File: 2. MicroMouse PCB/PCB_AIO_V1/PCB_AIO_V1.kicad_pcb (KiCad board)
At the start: 2 copper layers, 70 x 70 mm, 57 parts, among them J1 Conn_01x02_Pin, J10 Conn_01x03_Pin, J11 Conn_01x03_Pin, J12 Conn_01x03_Pin, J13 Conn_01x06_Pin, J14 Conn_01x06_Pin, J15 Conn_01x06_Pin, J16 Conn_01x06_Pin, J2 STLINK, J3 MPU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

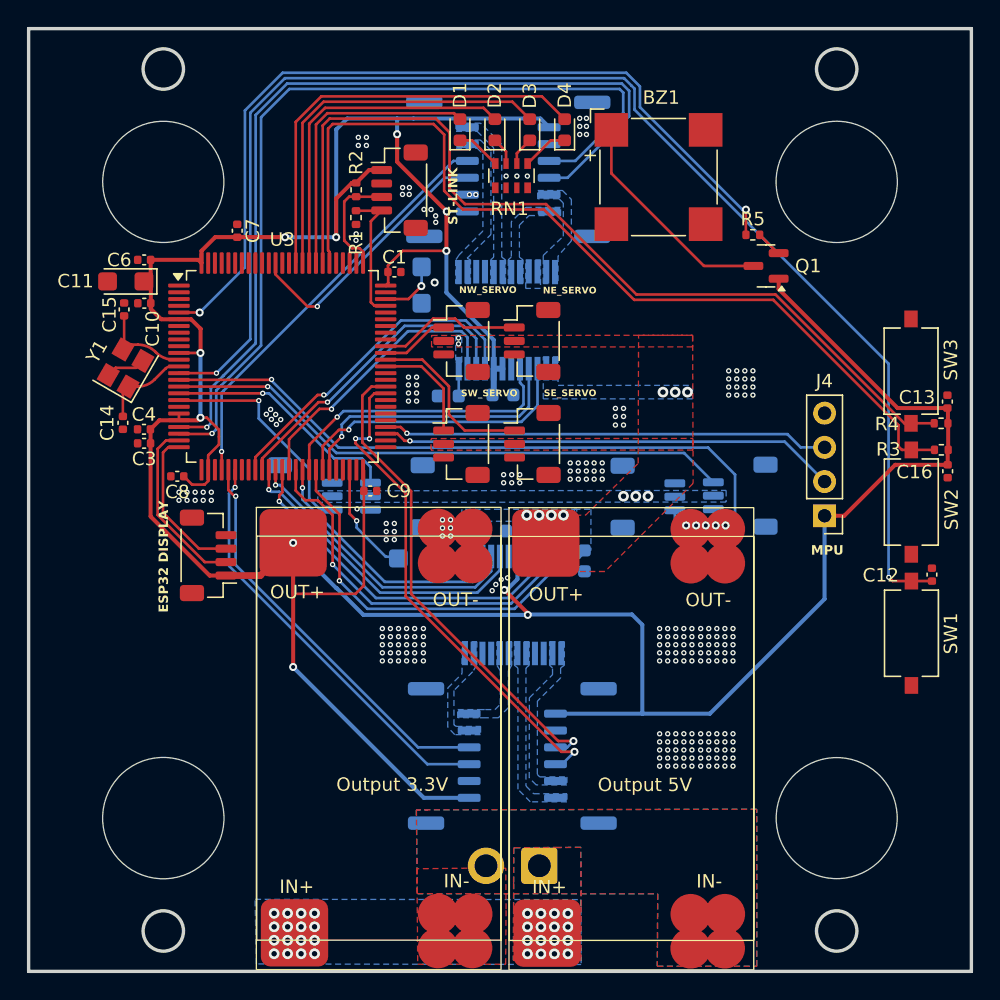
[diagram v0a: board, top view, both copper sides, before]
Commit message: moved stm32h743vit6
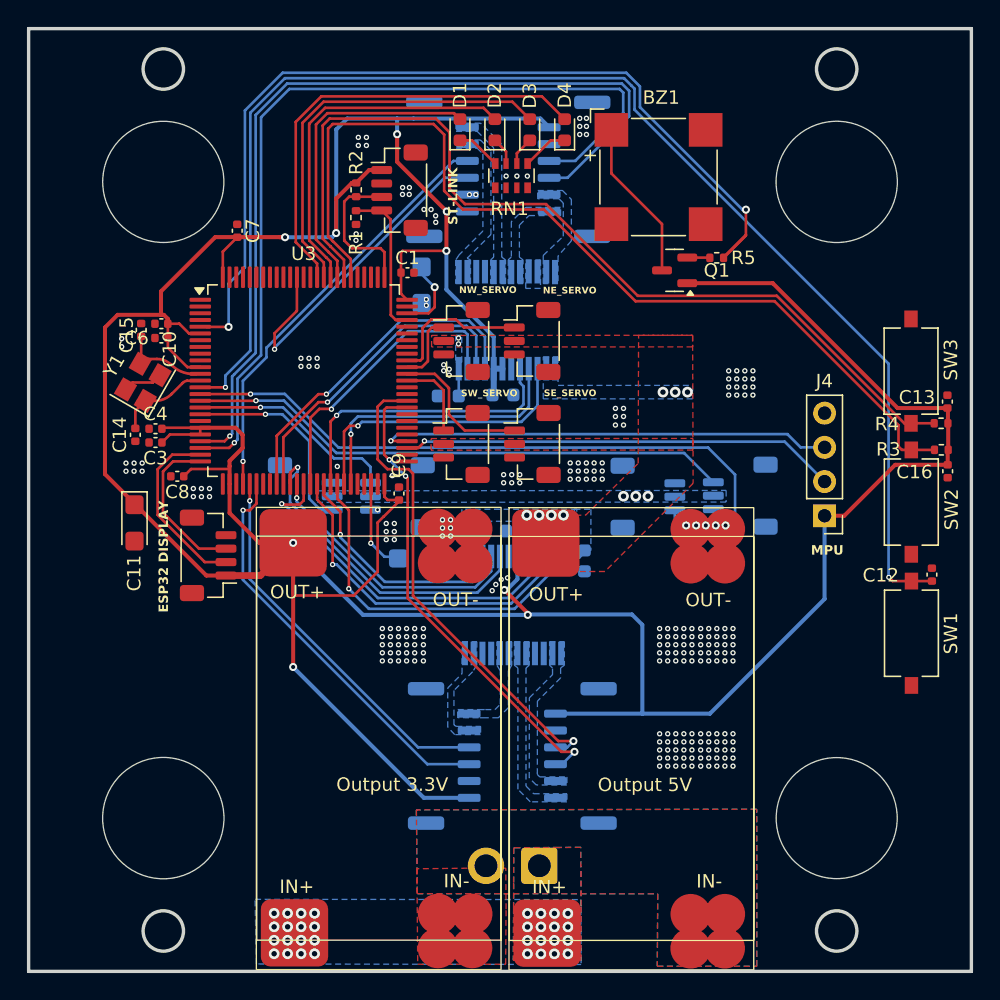
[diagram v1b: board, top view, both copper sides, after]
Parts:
- moved C11 17.9 mm to (126.6, 101.5), turned to -90 degrees
- moved Q1 6.79 mm to (166.7, 82.8)
- moved C6 5.94 mm to (128.6, 87.8)
- moved R5 3.18 mm to (169.9, 81.8), turned to 180 degrees
- moved C9 2.14 mm to (146.3, 99.3), turned to 90 degrees
- moved C10 1.98 mm to (128.6, 86.7)
- moved C15 1.98 mm to (127.1, 87.2)
- moved U3 1.90 mm to (139.2, 90.9)
- moved Y1 1.66 mm to (127.2, 91.1)
- moved C14 1.28 mm to (126.7, 95.0)
- moved C1 0.97 mm to (146.9, 82.9)
- moved C4 0.86 mm to (128.2, 94.5)
- moved C3 0.85 mm to (128.2, 95.5)
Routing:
- net +3.3V: track 277.8 -> 309.0 mm, vias 11 -> 9
- net /NW_ENC_B: track 20.1 -> 25.7 mm
- net /BUZZER: track 63.3 -> 68.3 mm
- net Net-(BZ1--): track 16.6 -> 12.0 mm
- net /SWCLK: track 8.41 -> 11.0 mm
- net /SE_ENC_A: track 37.8 -> 35.4 mm
- net /SE_IN2: track 27.7 -> 25.4 mm
- net /SW_SERVO: track 8.10 -> 6.00 mm
- net /SE_SERVO: track 13.0 -> 10.9 mm
- net /S_TOF: track 54.7 -> 52.6 mm
- net /N_TOF: track 18.2 -> 16.2 mm
- net /E_TOF: track 42.6 -> 40.6 mm
- net /SW_IN2: track 21.9 -> 20.0 mm
- net /SW_ENC_A: track 30.3 -> 28.5 mm
- net /SE_PWM: track 27.9 -> 26.1 mm
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
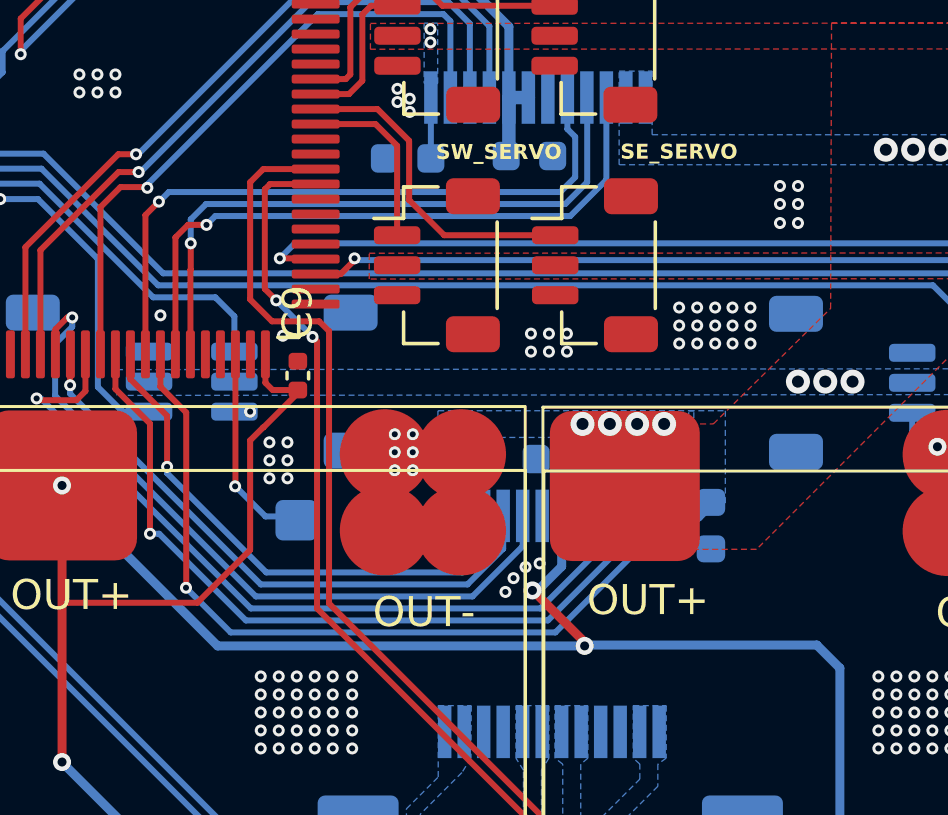
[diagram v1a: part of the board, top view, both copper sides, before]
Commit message: completed schematic of PCB_AIO_V2
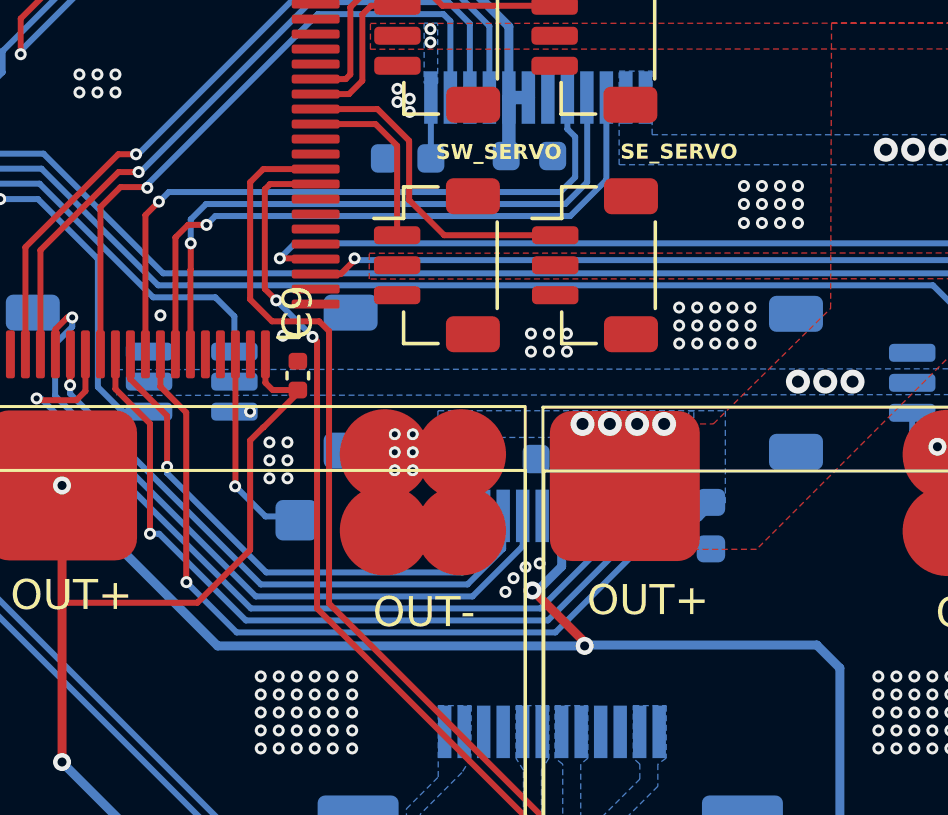
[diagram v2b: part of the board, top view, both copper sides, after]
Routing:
- net GND: vias 248 -> 254
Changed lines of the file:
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@@
 	)
 	(via
+		(at 161.14 93.599)
+		(size 0.4)
+		(drill 0.2)
+		(layers "F.Cu" "B.Cu")
+		(free yes)
+		(net 1)
+	)
+	(via
 		(at 167.422 119.56)
 		(size 0.4)
@@
 	)
 	(via
+		(at 161.74 94.234)
+		(size 0.4)
+		(drill 0.2)
+		(layers "F.Cu" "B.Cu")
+		(free yes)
+		(net 1)
+	)
+	(via
 		(at 145.634 111.147)
 		(size 0.4)
@@
 	)
 	(via
+		(at 161.14 92.999)
+		(size 0.4)
+		(drill 0.2)
+		(layers "F.Cu" "B.Cu")
+		(free yes)
+		(net 1)
+	)
+	(via
 		(at 169.87 119.56)
 		(size 0.4)
@@
 	)
 	(via
+		(at 161.74 92.999)
+		(size 0.4)
+		(drill 0.2)
+		(layers "F.Cu" "B.Cu")
+		(free yes)
+		(net 1)
+	)
+	(via
 		(at 140.19 89.28)
 		(size 0.4)
@@
 	)
 	(via
+		(at 161.74 93.599)
+		(size 0.4)
+		(drill 0.2)
+		(layers "F.Cu" "B.Cu")
+		(free yes)
+		(net 1)
+	)
+	(via
 		(at 154.04 97.92)
 		(size 0.4)
@@
 	)
 	(via
+		(at 161.14 94.234)
+		(size 0.4)
+		(drill 0.2)
+		(layers "F.Cu" "B.Cu")
+		(free yes)
+		(net 1)
+	)
+	(via
 		(at 148.3 84.91)
 		(size 0.4)
@@
 	)
 	(segment
-		(start 157.015 105.07)
-		(end 157.015 103.995)
+		(start 144.538628 107.48)
+		(end 154.605 107.48)
 		(width 0.2)
 		(layer "B.Cu")
@@
 	)
 	(segment
-		(start 154.605 107.48)
-		(end 157.015 105.07)
+		(start 141.648628 104.59)
+		(end 144.538628 107.48)
 		(width 0.2)
 		(layer "B.Cu")
@@
 	)
 	(segment
-		(start 141.648628 104.59)
-		(end 144.538628 107.48)
+		(start 154.605 107.48)
+		(end 157.015 105.07)
 		(width 0.2)
 		(layer "B.Cu")
@@
 	)
 	(segment
-		(start 144.538628 107.48)
-		(end 154.605 107.48)
+		(start 157.015 105.07)
+		(end 157.015 103.995)
 		(width 0.2)
 		(layer "B.Cu")
@@
 	)
 	(segment
-		(start 141.69 99.69)
-		(end 141.69 98.61)
+		(start 142.55 100.55)
+		(end 141.69 99.69)
 		(width 0.2)
 		(layer "F.Cu")
@@
 	)
 	(segment
-		(start 142.542169 106.39)
-		(end 142.55 106.382169)
+		(start 142.55 106.19848)
+		(end 142.55 100.55)
 		(width 0.2)
 		(layer "F.Cu")
@@
 	)
 	(segment
-		(start 142.55 106.382169)
-		(end 142.55 100.55)
+		(start 141.69 99.69)
+		(end 141.69 98.61)
 		(width 0.2)
 		(layer "F.Cu")
@@
 	)
 	(segment
-		(start 142.55 100.55)
-		(end 141.69 99.69)
+		(start 142.55576 106.20424)
+		(end 142.55 106.19848)
 		(width 0.2)
 		(layer "F.Cu")
@@
 	)
 	(via
-		(at 142.542169 106.39)
+		(at 142.55576 106.20424)
 		(size 0.4)
 		(drill 0.2)
@@
 	)
 	(segment
-		(start 154.855 107.88)
-		(end 157.665 105.07)
+		(start 142.55576 106.20424)
+		(end 144.23152 107.88)
 		(width 0.2)
 		(layer "B.Cu")
@@
 	)
 	(segment
-		(start 144.032169 107.88)
-		(end 154.855 107.88)
+		(start 157.665 105.07)
+		(end 157.665 103.995)
 		(width 0.2)
 		(layer "B.Cu")
@@
 	)
 	(segment
-		(start 157.665 105.07)
-		(end 157.665 103.995)
+		(start 144.23152 107.88)
+		(end 154.855 107.88)
 		(width 0.2)
 		(layer "B.Cu")
@@
 	)
 	(segment
-		(start 142.542169 106.39)
-		(end 144.032169 107.88)
+		(start 154.855 107.88)
+		(end 157.665 105.07)
 		(width 0.2)
 		(layer "B.Cu")
